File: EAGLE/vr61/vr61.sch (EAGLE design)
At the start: 231 parts, among them J6 MICROMOD-2222-C

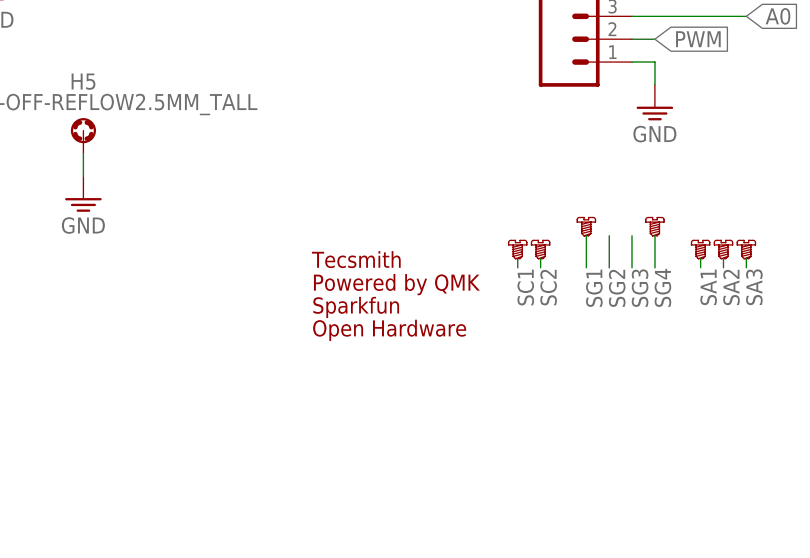
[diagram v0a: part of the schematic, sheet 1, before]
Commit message: correct micromod logo
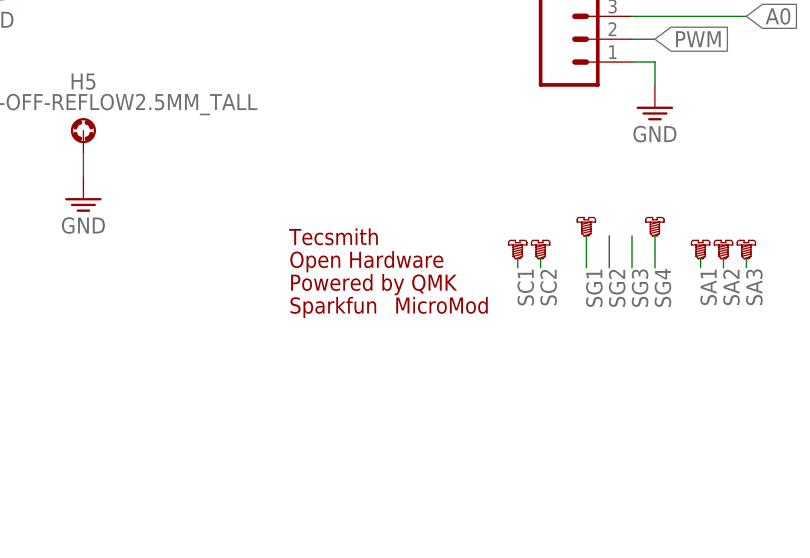
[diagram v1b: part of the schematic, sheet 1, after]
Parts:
- added U$3: MICROMOD-LOGO, random_logos:MICROMOD-LOGO
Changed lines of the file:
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@@
 <part name="U$6" library="random_logos" deviceset="QMK_LOGO" device=""/>
 <part name="U$8" library="random_logos" deviceset="TECSMITH-LOGO" device="LONG"/>
+<part name="U$3" library="random_logos" deviceset="MICROMOD-LOGO" device=""/>
 </parts>
 <sheets>
@@
 <instance part="SG1" gate="G$1" x="241.3" y="35.56" smashed="yes"/>
 <instance part="SG4" gate="G$1" x="248.92" y="35.56" smashed="yes"/>
-<instance part="LOGO1" gate="G$1" x="210.82" y="22.86" smashed="yes"/>
-<instance part="U$5" gate="G$1" x="210.82" y="25.4" smashed="yes"/>
-<instance part="U$6" gate="G$1" x="210.82" y="27.94" smashed="yes"/>
-<instance part="U$8" gate="G$1" x="210.82" y="30.48" smashed="yes"/>
+<instance part="LOGO1" gate="G$1" x="208.28" y="30.48" smashed="yes"/>
+<instance part="U$5" gate="G$1" x="208.28" y="25.4" smashed="yes"/>
+<instance part="U$6" gate="G$1" x="208.28" y="27.94" smashed="yes"/>
+<instance part="U$8" gate="G$1" x="208.28" y="33.02" smashed="yes"/>
+<instance part="U$3" gate="G$1" x="219.964" y="25.4" smashed="yes"/>
 </instances>
 <busses>

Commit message: updates after peer review on qmk discord
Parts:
- removed D62: 1N4148, adafruit:DIODESOD-123
- added D0: (no value), jlcpcb_basic_parts:1N5819WS
- R1, R2: value 1.5k -> 5.1K; device SparkFun-Resistors:1.5KOHM-0603-1/10W-1% -> rcl:R-EU_R0603
- R3: value 150k -> 150K; device SparkFun-Resistors:150KOHM-0603-1/10W-1% -> rcl:R-EU_R0603
- R4: device SparkFun-Resistors:75KOHM-0603-1/10W-1% -> rcl:R-EU_R0603
- renumbered U1 to LM1117
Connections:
- net VCC: now also D0.A; no longer D62.A
- net VSUP: now also D0.C; no longer D62.C
